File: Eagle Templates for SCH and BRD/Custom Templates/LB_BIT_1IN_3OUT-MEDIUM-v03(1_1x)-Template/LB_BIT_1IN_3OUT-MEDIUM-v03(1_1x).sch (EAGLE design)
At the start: 24 parts, among them U1 LV321SOT23-5, U2 LV321SOT23-5, U3 LV321SOT23-5, U6 LV321SOT23-5

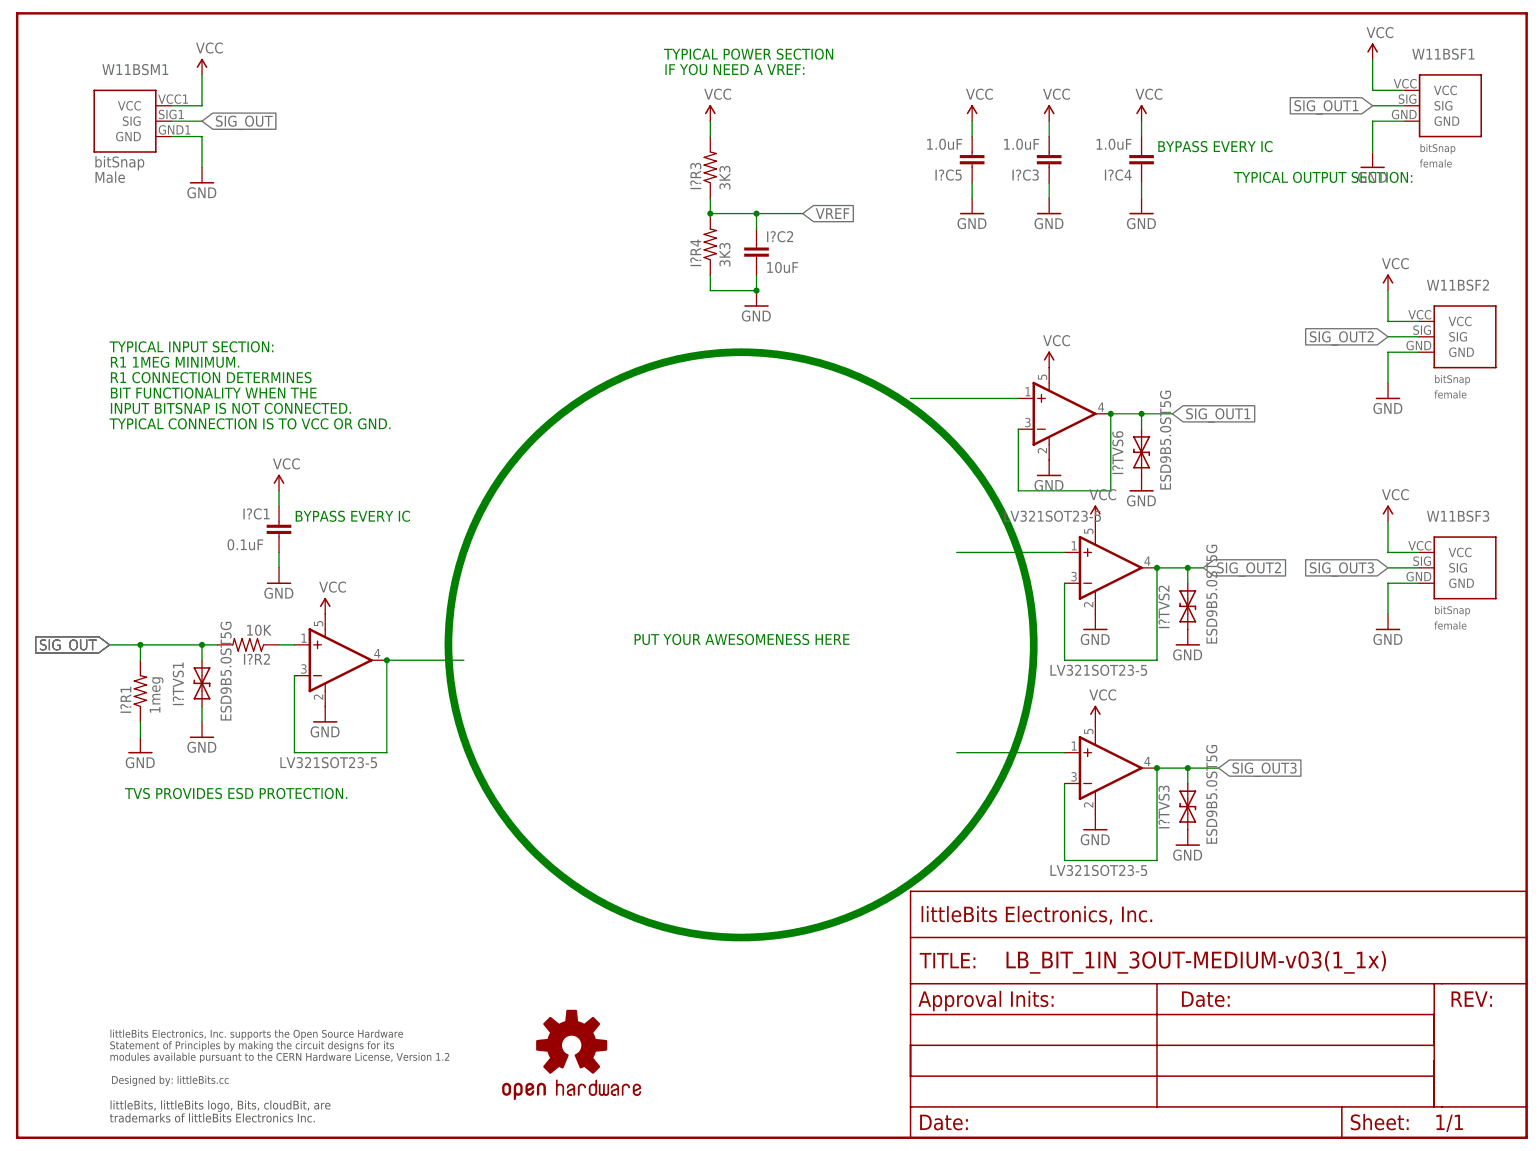
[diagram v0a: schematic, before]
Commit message: Updated templates
- Added ferrite beads
- Moved text and annotations off of Nets layer
- Minor layout changes
- Removed I/O/W prefix from reference designators
- Removed output stage components from output bits
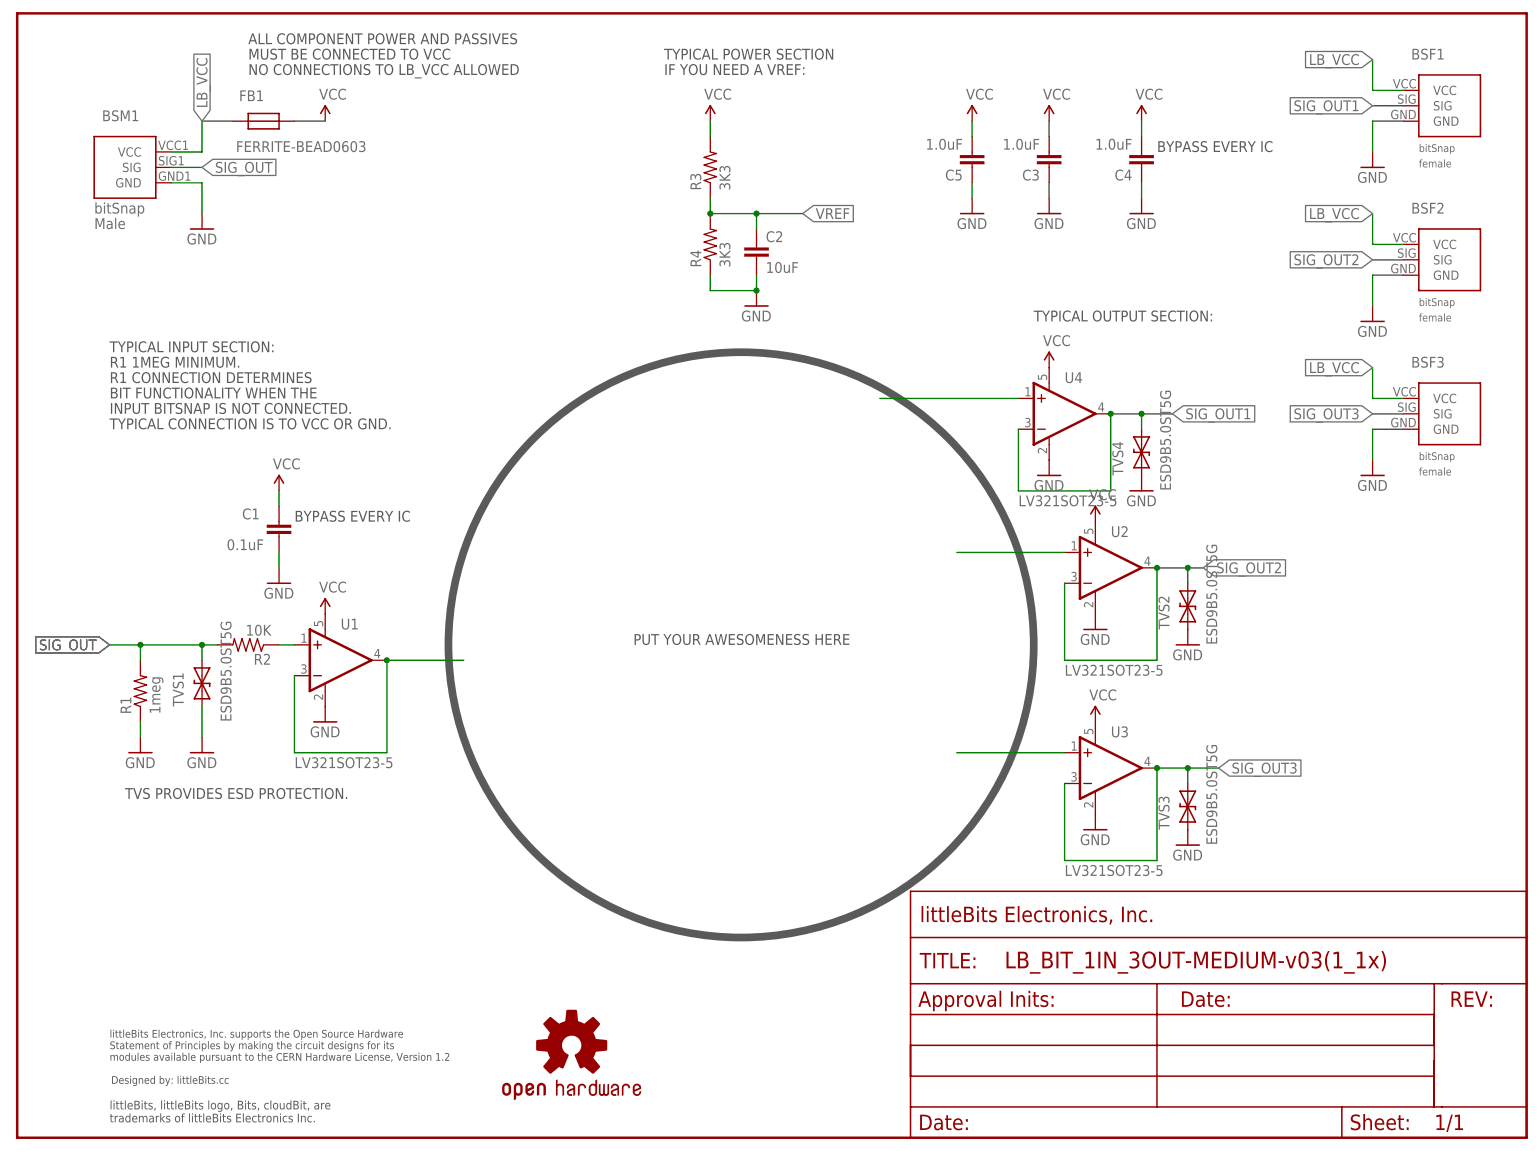
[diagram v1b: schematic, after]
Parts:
- removed W11BSF1, W11BSF2, W11BSF3: BITSNAP_V03_FEMALE, bitSnap:BITSNAP_V03_FEMALE
- removed W11BSM1: BITSNAP_V03_MALE, bitSnap:BITSNAP_V03_MALE
- added BSF1, BSF2, BSF3: BITSNAP_V03_FEMALE, bitSnap:BITSNAP_V03_FEMALE
- added BSM1: BITSNAP_V03_MALE, bitSnap:BITSNAP_V03_MALE
- added FB1: FERRITE-BEAD0603, LITTLEBITS:FERRITE-BEAD0603
- renumbered I?C1 to C1, I?C2 to C2, I?C3 to C3, I?C4 to C4, I?C5 to C5, I?R1 to R1, I?R2 to R2, I?R3 to R3, I?R4 to R4, I?TVS1 to TVS1, I?TVS2 to TVS2, I?TVS3 to TVS3, I?TVS6 to TVS4, U6 to U4
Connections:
- new net LB_VCC: BSF1.VCC, BSF2.VCC, BSF3.VCC, BSM1.VCC, FB1.P$2
- net GND: now also BSF1.GND, BSF2.GND, BSF3.GND, BSM1.GND; no longer W11BSF2.GND, W11BSF3.GND, W11BSM1.GND
- net SIG_OUT: now also BSM1.SIG; no longer W11BSM1.SIG
- net SIG_OUT1: now also BSF1.SIG
- net SIG_OUT2: now also BSF2.SIG; no longer W11BSF2.SIG
- net SIG_OUT3: now also BSF3.SIG; no longer W11BSF3.SIG
- net VCC: now also FB1.P$1; no longer W11BSF2.VCC, W11BSF3.VCC, W11BSM1.VCC
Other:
- note added: "ALL COMPONENT POWER AND PASSIVES"
- note added: "MUST BE CONNECTED TO VCC"
- note added: "NO CONNECTIONS TO LB_VCC ALLOWED"
